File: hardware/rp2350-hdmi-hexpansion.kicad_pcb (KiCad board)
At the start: 4 copper layers, 32 x 36.6 mm, 90 parts, among them J1 Hexpansion-Connector, J2 USB-C, J3 SWD, J4 Qwiic, J5 HDMI-A, SW1 BOOTSEL, SW2 RESET, U1 RP2354A, U10 ZD24C64A (fallback), U11 SN74LVC1G07, U2 TPS2116DRLR, U3 TLV62569DBVR, U4 TPS61023DRLR, U6 TPD4E05U06, U7 TPD4E05U06, U8 USBLC6-2SC6, U9 APS6404L-3SQR-SN, Y1 12MHz

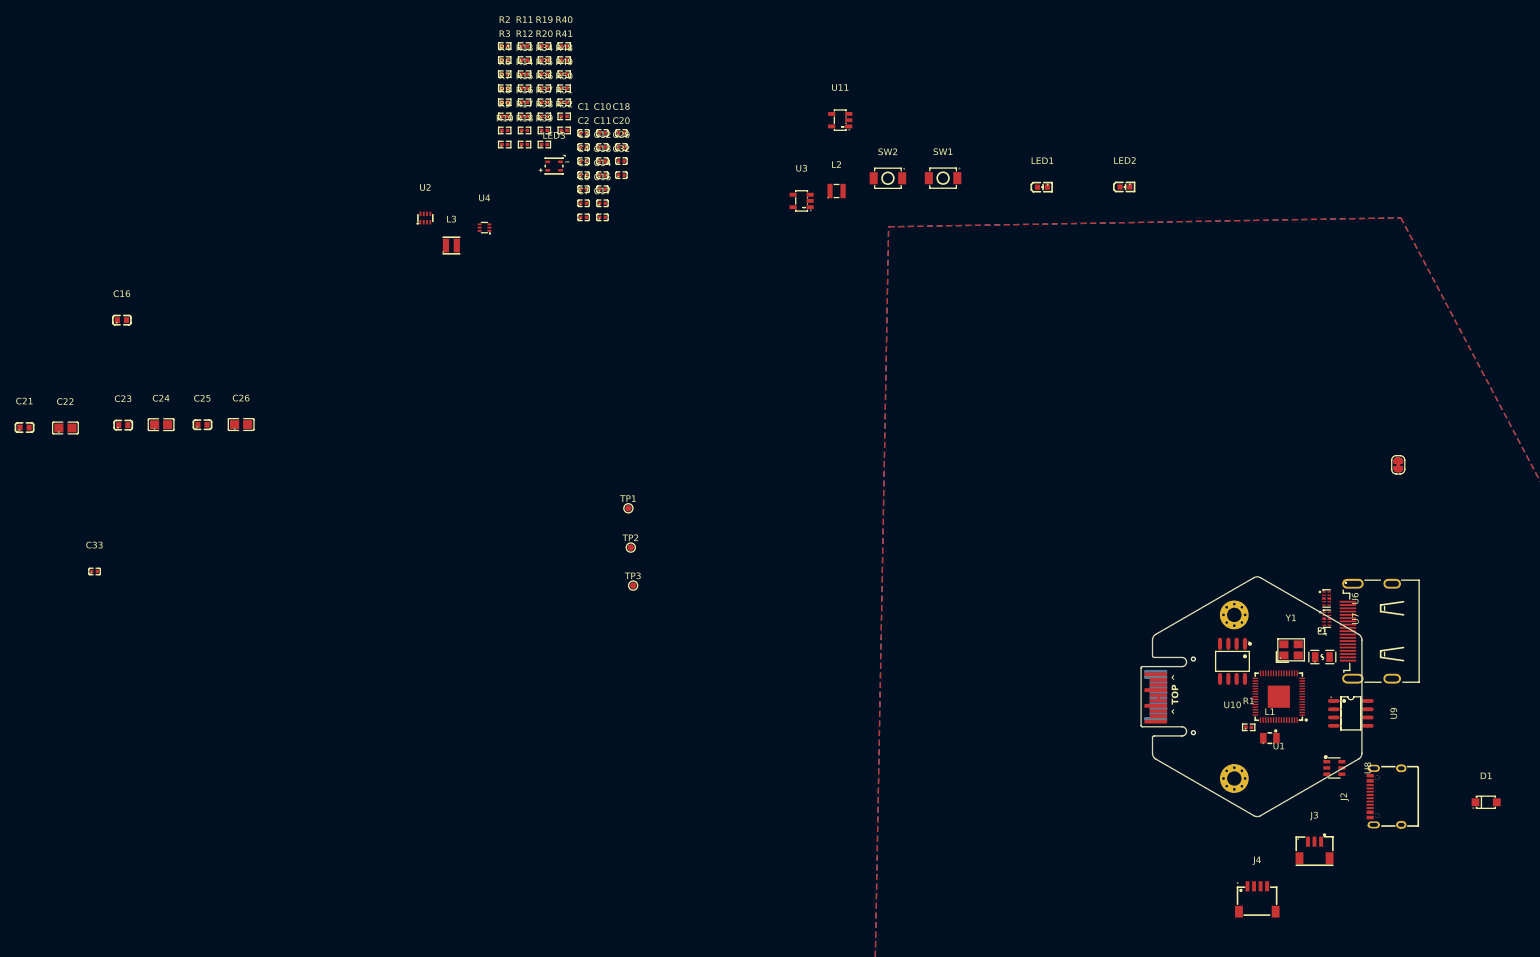
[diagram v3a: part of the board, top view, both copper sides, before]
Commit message: hardware: USB-C removed, 4-layer HDMI rules, smaller silk, SK6805 3D model
- Remove USB-C socket and dependent circuitry from the design
- Add HDMI_TMDS net class (0.15 mm / 0.25 mm gap) for the HDMI pairs
- Reference designator silk text reduced to 0.6 mm
- SK6805 footprint now references lib/jlc.3dshapes/SK6805MICRO-J.step
  (STEP files are gitignored; add the model locally)

Co-Authored-By: Claude Sonnet 5.5 <noreply@anthropic.com>
Claude-Session: https://claude.ai/code/session_01VMD2iSg4JfioYFvgvvdo7j
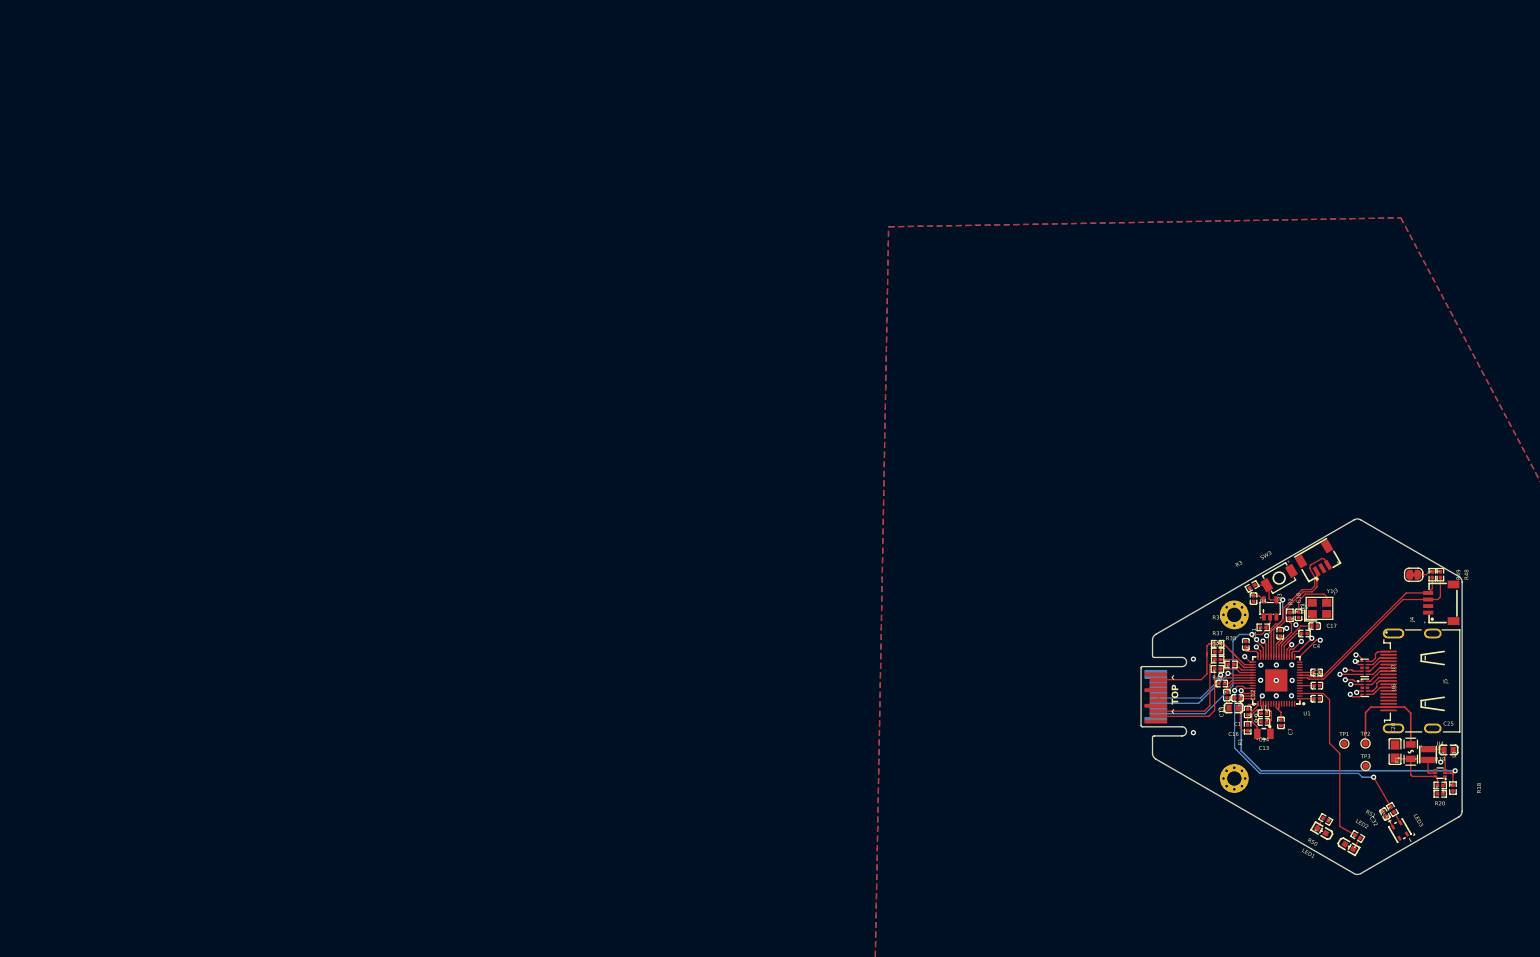
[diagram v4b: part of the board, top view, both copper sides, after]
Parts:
- removed C20, C29: 100nF, jlc:C0402
- removed C21, C23: 10uF, jlc:C0603
- removed C22, C24: 22uF, jlc:C0805
- removed D1: SMF5.0A, jlc:SOD-123FL_L2.7-W1.8-LS3.8-RD
- removed J2: USB-C, jlc:USB-C-SMD_TYPE-C-16PIN-2MD-073
- removed L2: 2.2uH, jlc:IND-SMD_L2.5-W2.0_MHCHL2520
- removed R10, R11: 27R, jlc:R0402
- removed R12, R16, R17, R34, R35: 100k, jlc:R0402
- removed R13, R15: 22k, jlc:R0402
- removed R14: 33k, jlc:R0402
- removed R40, R6: 1k, jlc:R0402
- removed R7: 10k, jlc:R0402
- removed R8, R9: 5.1k, jlc:R0402
- removed SW1: BOOTSEL, jlc:SW-SMD_L3.9-W3.0-P4.45
- removed SW2: RESET, jlc:SW-SMD_L3.9-W3.0-P4.45
- removed U10: ZD24C64A (fallback), jlc:SOP-8_L4.9-W3.9-P1.27-LS6.0-BL
- removed U2: TPS2116DRLR, jlc:SOT-583-8_L2.1-W1.6-P0.50-LS1.6-BL
- removed U3: TLV62569DBVR, jlc:SOT-23-5_L3.0-W1.7-P0.95-LS2.8-BR
- removed U8: USBLC6-2SC6, jlc:SOT-23-6_L2.9-W1.6-P0.95-LS2.8-BL
- removed U9: APS6404L-3SQR-SN, jlc:SOIC-8_L4.9-W3.9-P1.27-LS6.0-BL
- added SW3: RESET, jlc:SW-SMD_L3.9-W3.0-P4.45, F.Cu at (119.4, 81.9)
- moved C25 196.8 mm to (145.2, 108.1)
- moved C26 183.3 mm to (137.1, 108.4), turned to 90 degrees
- moved C16 179.9 mm to (112.4, 101.7), turned to 180 degrees
- moved R19 177.5 mm to (144.0, 113.6)
- moved C33 177.1 mm to (115.4, 85.0), turned to -90 degrees
- moved R20 176.9 mm to (144.0, 114.8), turned to 180 degrees
- moved R18 172.6 mm to (145.9, 114.0), turned to -90 degrees
- moved L3 168.3 mm to (142.1, 108.8), turned to -90 degrees
- moved U4 168.2 mm to (144.0, 111.7)
- moved LED3 164.4 mm to (137.8, 120.5), turned to -60 degrees
- moved R51 163.7 mm to (131.3, 121.4), turned to -30 degrees
- moved R52 163.7 mm to (136.7, 117.2), turned to -60 degrees
- moved R50 159.8 mm to (126.5, 118.8), turned to 150 degrees
- moved R48 154.2 mm to (144.0, 81.3), turned to -90 degrees
- moved C32 152.1 mm to (135.5, 117.9), turned to 120 degrees
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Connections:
- net /+3V3 renamed +3V3
- net /GND renamed GND
- net /RGB_DIN_R renamed Net-(LED3-DIN)
- J1 pad 3: /LS_B -> unconnected-(J1-LS_B-Pad3)
- J5 pad 19: /HDMI_HPD -> unconnected-(J5-HotPlugDetect-Pad19)
- U6 pad 1: /HDMI_D2_P -> /HDMI_D0_P
- U6 pad 10: /HDMI_D2_P -> /HDMI_D0_P
- U6 pad 2: /HDMI_D2_N -> /HDMI_D0_N
- U6 pad 9: /HDMI_D2_N -> /HDMI_D0_N
- U7 pad 1: /HDMI_D1_P -> /HDMI_D2_P
- U7 pad 10: /HDMI_D1_P -> /HDMI_D2_P
- U7 pad 2: /HDMI_D1_N -> /HDMI_D2_N
- U7 pad 4: /HDMI_D0_P -> /HDMI_D1_P
- U7 pad 5: /HDMI_D0_N -> /HDMI_D1_N
- U7 pad 6: /HDMI_D0_N -> /HDMI_D1_N
- U7 pad 7: /HDMI_D0_P -> /HDMI_D1_P
- U7 pad 9: /HDMI_D1_N -> /HDMI_D2_N
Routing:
- net /BOOST_EN: track 0.00 -> 49.4 mm, vias 0 -> 2
- net +3V3: track 0.00 -> 37.9 mm
- net /RGB_DIN: track 0.00 -> 35.2 mm, vias 0 -> 2
- net /QWIIC_SDA: track 0.00 -> 29.7 mm
- net /LS_A: track 0.00 -> 28.0 mm, vias 0 -> 1
- net /QWIIC_SCL: track 0.00 -> 27.6 mm
- net /HDMI_D0_N: track 0.00 -> 25.0 mm, vias 0 -> 2
- net /HDMI_D1_N: track 0.00 -> 25.0 mm, vias 0 -> 2
- net /HDMI_D0_P: track 0.00 -> 24.0 mm, vias 0 -> 2
- net /HDMI_D1_P: track 0.00 -> 23.5 mm, vias 0 -> 2
- net /HDMI_CK_N: track 0.00 -> 23.3 mm, vias 0 -> 2
- net /LED_STATUS: track 0.00 -> 23.2 mm
- net /HDMI_CK_P: track 0.00 -> 22.4 mm, vias 0 -> 2
- net /HDMI_D2_P: track 0.00 -> 18.4 mm, vias 0 -> 2
- net /HDMI_D2_N: track 0.00 -> 18.1 mm, vias 0 -> 2
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- added copper zone on In1.Cu, net GND
- added copper zone on In2.Cu, net GND
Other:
- board size 32 x 36.6 mm -> 47.3 x 54.3 mm

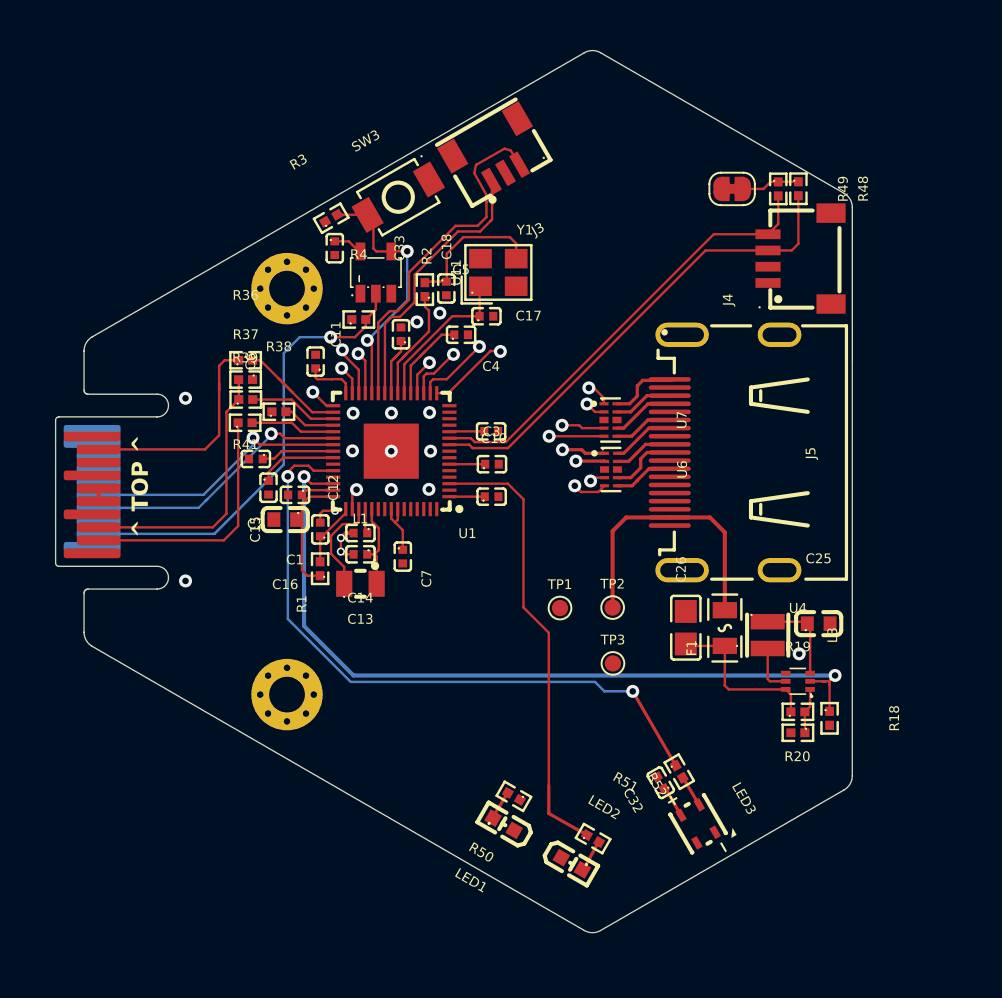
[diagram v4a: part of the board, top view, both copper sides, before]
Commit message: hardware: C13/C14 to 0603 (CL10A475KO8NNNC, C19666) to make room for a trace
Co-Authored-By: Claude Sonnet 5.5 <noreply@anthropic.com>
Claude-Session: https://claude.ai/code/session_01VMD2iSg4JfioYFvgvvdo7j
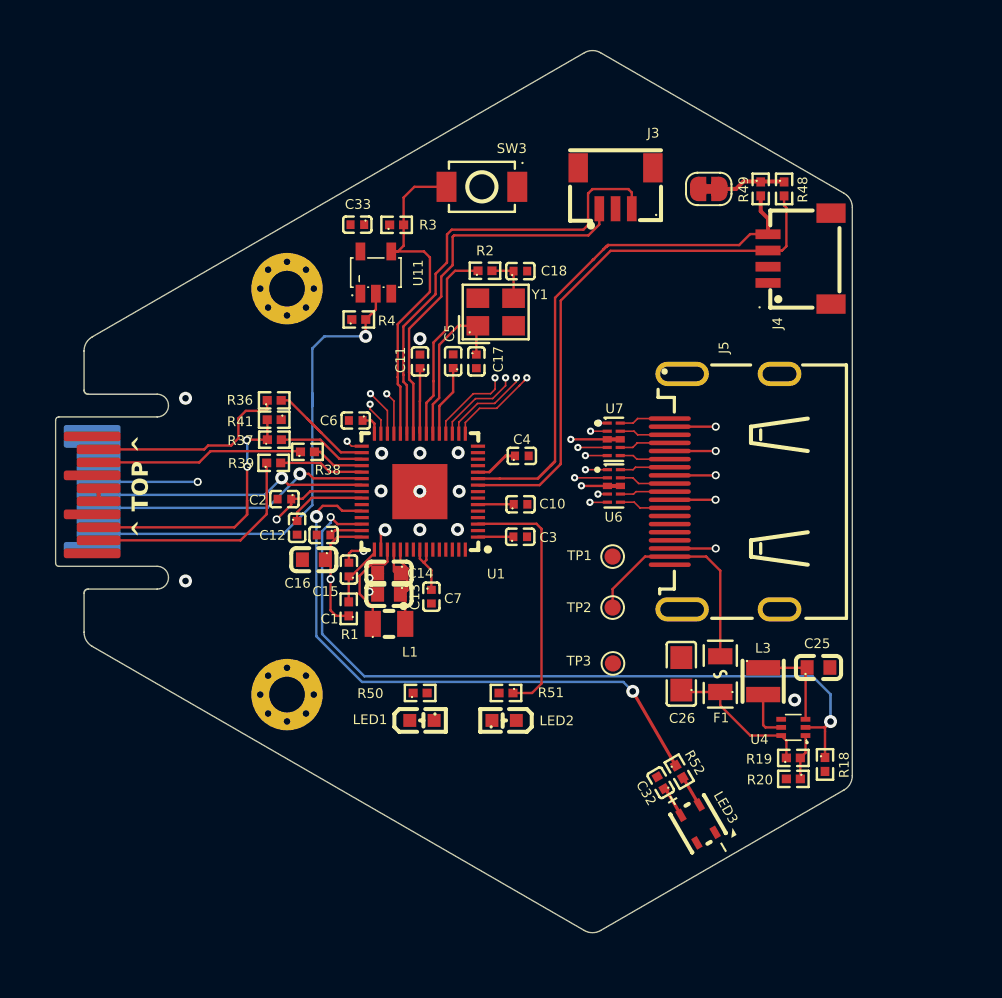
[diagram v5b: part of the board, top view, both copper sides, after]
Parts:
- C13, C14: footprint jlc:C0402 -> jlc:C0603
- moved R51 10.4 mm to (126.0, 112.4), turned to 180 degrees
- moved LED2 9.76 mm to (125.9, 114.1), turned to 180 degrees
- moved R50 8.60 mm to (120.7, 112.4), turned to 0 degrees
- moved LED1 8.14 mm to (120.8, 114.1), turned to 0 degrees
- moved J3 7.68 mm to (132.7, 81.3), turned to 180 degrees
- moved SW3 5.19 mm to (124.5, 81.2), turned to 0 degrees
- moved C18 4.68 mm to (126.9, 86.4), turned to 0 degrees
- moved TP1 4.53 mm to (132.6, 104.0)
- moved C6 4.39 mm to (116.7, 95.6), turned to 180 degrees
- moved R3 4.05 mm to (119.2, 83.6), turned to 0 degrees
- moved R2 3.88 mm to (124.7, 86.4), turned to 0 degrees
- moved U1 3.05 mm to (120.7, 100.0)
- moved C1 3.03 mm to (114.8, 102.7)
- moved C12 3.03 mm to (113.1, 102.2)
- moved C13 3.03 mm to (118.8, 106.3)
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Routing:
- net GND: track 5.63 -> 31.3 mm, vias 17 -> 24
- net /HS_G: track 0.00 -> 12.7 mm
- net /SWDIO: track 15.7 -> 28.2 mm
- net /LED_STATUS: track 23.2 -> 15.6 mm
- net /SWCLK: track 16.9 -> 23.7 mm
- net /QWIIC_SCL: track 27.6 -> 33.5 mm
- net /XOUT_XTAL: track 8.82 -> 3.01 mm
- net /RUN: track 16.1 -> 21.0 mm, vias 2 -> 0
- net /XOUT: track 7.27 -> 12.2 mm
- net /QWIIC_SDA: track 29.7 -> 34.1 mm
- net /RGB_DIN: track 35.2 -> 31.6 mm
- net /V5_HDMI: track 17.1 -> 14.2 mm
- net /LS_A: track 28.0 -> 30.8 mm
- net /HDMI_D2_P: track 18.4 -> 15.7 mm
- net /HDMI_CK_P: track 22.4 -> 20.6 mm
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
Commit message: hardware: save latest KiCad state (PCB layout, view settings)
Co-Authored-By: Claude Sonnet 5.5 <noreply@anthropic.com>
Claude-Session: https://claude.ai/code/session_01VMD2iSg4JfioYFvgvVDo7J
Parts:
- moved L1 1.00 mm to (118.7, 109.1)
- moved C13 0.83 mm to (118.7, 107.2)
- moved C14 0.39 mm to (118.7, 105.4)
- moved C7 0.34 mm to (121.7, 106.6)
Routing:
- net /DVDD: track 16.5 -> 18.4 mm
- net GND: track 31.3 -> 32.2 mm, vias 24 -> 22
- net +3V3: track 37.2 -> 37.9 mm
